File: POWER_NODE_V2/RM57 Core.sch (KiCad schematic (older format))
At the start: 4 parts, among them J5 Booster_J1_J3, J6 I2C2_J10_8_9, J7 Booster_J4_J2

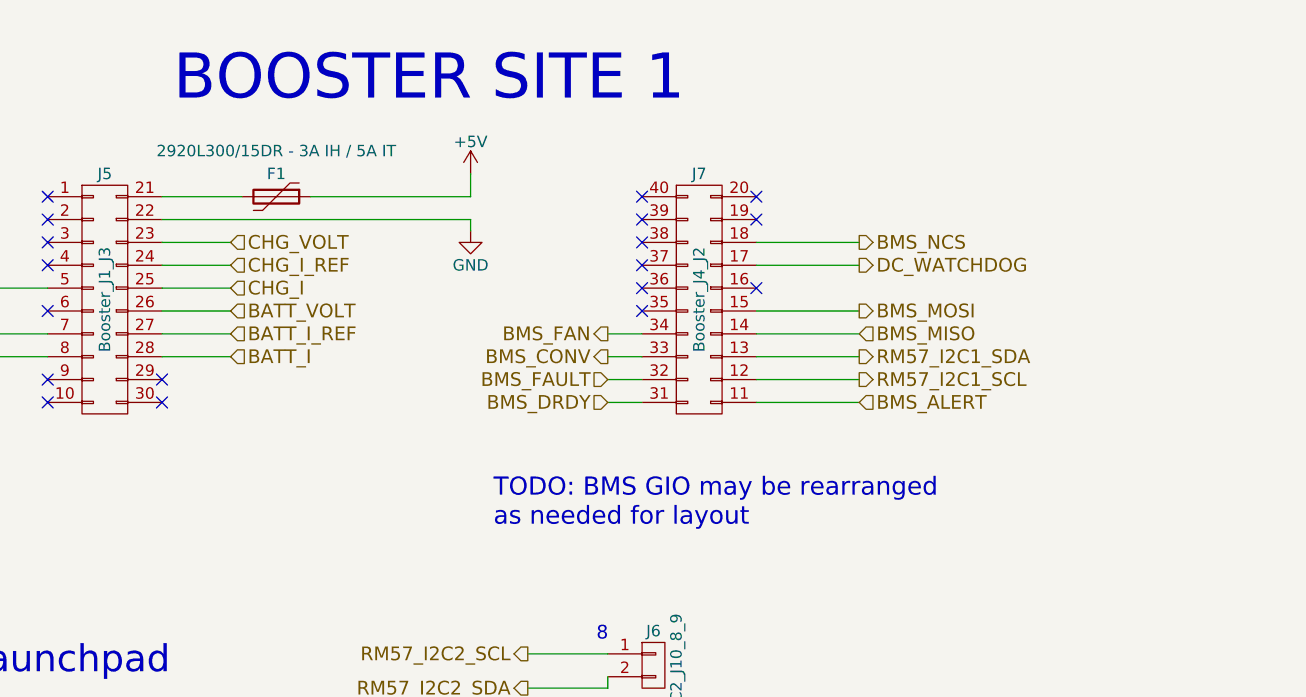
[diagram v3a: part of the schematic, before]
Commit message: Power Node v2 WIP
TODO: 3d models, double check everything, update connector P/N on
schematics, align boards and drill holes
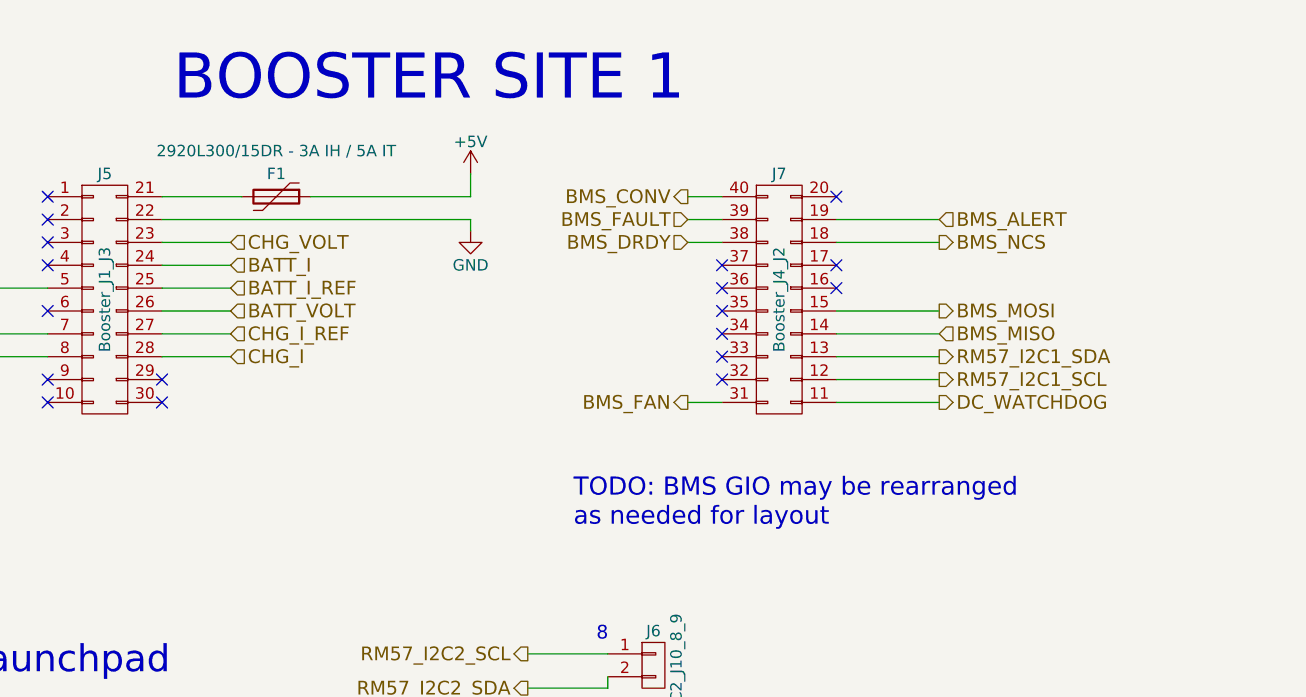
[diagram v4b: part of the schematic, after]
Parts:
- J5: footprint Pin_Headers:Pin_Header_Straight_2x10_Pitch2.54mm -> rLoop Footprints:Booster1_Header_J1_J3
- J6: footprint Pin_Headers:Pin_Header_Straight_1x02_Pitch2.54mm -> Pin_Headers:Pin_Header_Straight_1x02_Pitch2.54mm_SMD_Pin1Left
- J7: footprint Pin_Headers:Pin_Header_Straight_2x10_Pitch2.54mm -> rLoop Footprints:Booster1_J4_J2
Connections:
- net BATT_I: now also J5.24 (P24); no longer J5.28 (P28)
- net BATT_I_REF: now also J5.25 (P25); no longer J5.27 (P27)
- net BMS_ALERT: now also J7.19 (P19); no longer J7.11 (P11)
- net BMS_CONV: now also J7.40 (P40); no longer J7.33 (P33)
- net BMS_DRDY: now also J7.38 (P38); no longer J7.31 (P31)
- net BMS_FAN: now also J7.31 (P31); no longer J7.34 (P34)
- net BMS_FAULT: now also J7.39 (P39); no longer J7.32 (P32)
- net CHG_I: now also J5.28 (P28); no longer J5.25 (P25)
- net CHG_I_REF: now also J5.27 (P27); no longer J5.24 (P24)
- net DC_WATCHDOG: now also J7.11 (P11); no longer J7.17 (P17)
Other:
- moved on the sheet: J7
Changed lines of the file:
@@
 Text HLabel 3700 3200 0    60   Output ~ 0
 CHG_RLY
-Text HLabel 5200 2800 2    60   Input ~ 0
+Text HLabel 5200 3100 2    60   Input ~ 0
 CHG_I_REF
 Text HLabel 5200 2700 2    60   Input ~ 0
@@
 Text HLabel 5200 3000 2    60   Input ~ 0
 BATT_VOLT
-Text HLabel 7950 2800 2    60   Output ~ 0
+Text HLabel 8300 3400 2    60   Output ~ 0
 DC_WATCHDOG
 Text HLabel 3700 3100 0    60   Output ~ 0
 BMS_SCK
-Text HLabel 7950 3000 2    60   Output ~ 0
+Text HLabel 8300 3000 2    60   Output ~ 0
 BMS_MOSI
-Text HLabel 7950 2700 2    60   Output ~ 0
+Text HLabel 8300 2700 2    60   Output ~ 0
 BMS_NCS
-Text HLabel 7950 3100 2    60   Input ~ 0
+Text HLabel 8300 3100 2    60   Input ~ 0
 BMS_MISO
-Text HLabel 6850 3400 0    60   Input ~ 0
+Text HLabel 7200 2700 0    60   Input ~ 0
 BMS_DRDY
 Text HLabel 3700 2900 0    60   Output ~ 0
 BMS_COMMS_EN
-Text HLabel 6850 3200 0    60   Output ~ 0
+Text HLabel 7200 2500 0    60   Output ~ 0
 BMS_CONV
-Text HLabel 7950 3200 2    60   Output ~ 0
+Text HLabel 8300 3200 2    60   Output ~ 0
 RM57_I2C1_SDA
-Text HLabel 7950 3300 2    60   Output ~ 0
+Text HLabel 8300 3300 2    60   Output ~ 0
 RM57_I2C1_SCL
 Text HLabel 6500 4650 0    60   Output ~ 0
@@
 Text HLabel 6500 4500 0    60   Output ~ 0
 RM57_I2C2_SCL
-Text HLabel 6850 3100 0    60   Output ~ 0
+Text HLabel 7200 3400 0    60   Output ~ 0
 BMS_FAN
-Text HLabel 6850 3300 0    60   Input ~ 0
+Text HLabel 7200 2600 0    60   Input ~ 0
 BMS_FAULT
-Text HLabel 7950 3400 2    60   Input ~ 0
+Text HLabel 8300 2600 2    60   Input ~ 0
 BMS_ALERT
 $Comp
@@
 F 0 "J6" H 7050 4700 50  0000 C CNN
 F 1 "I2C2_J10_8_9" V 7150 4550 50  0000 C CNN
-F 2 "Pin_Headers:Pin_Header_Straight_1x02_Pitch2.54mm" H 7050 4550 50  0001 C CNN
+F 2 "Pin_Headers:Pin_Header_Straight_1x02_Pitch2.54mm_SMD_Pin1Left" H 7050 4550 50  0001 C CNN
 F 3 "" H 7050 4550 50  0001 C CNN
 	1    7050 4550
@@
 F 0 "J5" H 4650 3500 50  0000 C CNN
 F 1 "Booster_J1_J3" V 4650 2950 50  0000 C CNN
-F 2 "Pin_Headers:Pin_Header_Straight_2x10_Pitch2.54mm" H 4650 1750 50  0001 C CNN
+F 2 "rLoop Footprints:Booster1_Header_J1_J3" H 4650 1750 50  0001 C CNN
 F 3 "" H 4650 1750 50  0001 C CNN
 	1    4650 2950
 	1    0    0    -1
 $EndComp
-$Comp
-L Booster_J4_J2 J7
-U 1 1 5950B1BF
-P 7250 2950
-F 0 "J7" H 7250 3500 50  0000 C CNN
-F 1 "Booster_J4_J2" V 7250 2950 50  0000 C CNN
-F 2 "Pin_Headers:Pin_Header_Straight_2x10_Pitch2.54mm" H 7250 1750 50  0001 C CNN
-F 3 "" H 7250 1750 50  0001 C CNN
-	1    7250 2950
-	1    0    0    -1
-$EndComp
-Wire Wire Line
-	7950 3300 7500 3300
-Wire Wire Line
-	7500 3200 7950 3200
-Wire Wire Line
-	7950 3100 7500 3100
-Wire Wire Line
-	7500 3000 7950 3000
-Wire Wire Line
-	7950 2700 7500 2700
+Wire Wire Line
+	8300 3300 7850 3300
+Wire Wire Line
+	8300 3100 7850 3100
+Wire Wire Line
+	7850 3000 8300 3000
+Wire Wire Line
+	8300 2700 7850 2700
 Wire Wire Line
 	3700 3100 4400 3100
@@
 Text Notes 6800 4800 0    60   ~ 0
 9
+Text HLabel 5200 3200 2    60   Input ~ 0
+CHG_I
 Text HLabel 5200 2900 2    60   Input ~ 0
-CHG_I
-Text HLabel 5200 3100 2    60   Input ~ 0
 BATT_I_REF
-Text HLabel 5200 3200 2    60   Input ~ 0
+Text HLabel 5200 2800 2    60   Input ~ 0
 BATT_I
-Text Notes 6350 3950 0    79   ~ 0
+Text Notes 6700 3950 0    79   ~ 0
 TODO: BMS GIO may be rearranged\nas needed for layout
 Wire Wire Line
-	6850 3100 7000 3100
-Wire Wire Line
-	7000 3200 6850 3200
-Wire Wire Line
-	6850 3300 7000 3300
-Wire Wire Line
-	7000 3400 6850 3400
-Wire Wire Line
-	7500 3400 7950 3400
-Wire Wire Line
-	4900 3200 5200 3200
-Wire Wire Line
-	5200 3100 4900 3100
-Wire Wire Line
 	4900 3000 5200 3000
-Wire Wire Line
-	5200 2900 4900 2900
-Wire Wire Line
-	4900 2800 5200 2800
-Wire Wire Line
-	5200 2700 4900 2700
-Wire Wire Line
-	7950 2800 7500 2800
 Wire Wire Line
 	3700 2900 4400 2900
@@
 	1    0    0    -1
 $EndComp
-NoConn ~ 7000 3000
-NoConn ~ 7000 2900
-NoConn ~ 7000 2800
-NoConn ~ 7000 2700
-NoConn ~ 7000 2600
-NoConn ~ 7000 2500
-NoConn ~ 7500 2500
-NoConn ~ 7500 2600
-NoConn ~ 7500 2900
+NoConn ~ 7350 3000
+NoConn ~ 7350 2900
+NoConn ~ 7850 2500
+NoConn ~ 7850 2900
 $Comp
 L Polyfuse F1
@@
 Text Notes 2900 4600 0    118  ~ 0
 J9 Pins 8,9 on Launchpad
+Wire Wire Line
+	5200 2700 4900 2700
+Wire Wire Line
+	5200 2800 4900 2800
+Wire Wire Line
+	4900 2900 5200 2900
+Wire Wire Line
+	5200 3100 4900 3100
+Wire Wire Line
+	4900 3200 5200 3200
+Wire Wire Line
+	7850 3200 8300 3200
+Wire Wire Line
+	7850 2600 8300 2600
+Wire Wire Line
+	7200 2500 7350 2500
+Wire Wire Line
+	7350 2600 7200 2600
+Wire Wire Line
+	7200 2700 7350 2700
+NoConn ~ 7850 2800
+Wire Wire Line
+	7850 3400 8300 3400
+NoConn ~ 7350 3200
+NoConn ~ 7350 3300
+$Comp
+L Booster_J4_J2 J7
+U 1 1 5950B1BF
+P 7600 2950
+F 0 "J7" H 7600 3500 50  0000 C CNN
+F 1 "Booster_J4_J2" V 7600 2950 50  0000 C CNN
+F 2 "rLoop Footprints:Booster1_J4_J2" H 7600 1750 50  0001 C CNN
+F 3 "" H 7600 1750 50  0001 C CNN
+	1    7600 2950
+	1    0    0    -1
+$EndComp
+Wire Wire Line
+	7200 3400 7350 3400
+NoConn ~ 7350 3100
+NoConn ~ 7350 2800
 $EndSCHEMATC

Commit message: Lot's of progress
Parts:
- J5: value Booster_J1_J3 -> 5-146130-9; footprint rLoop Footprints:Booster1_Header_J1_J3 -> rLoop_Footprints:Booster1_Header_J1_J3
- J7: value Booster_J4_J2 -> 5-146130-9; footprint rLoop Footprints:Booster1_J4_J2 -> rLoop_Footprints:Booster1_J4_J2
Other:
- note added: "J1 & J3"
- note added: "J2 & J4"
- note removed: "TODO: BMS GIO may be rearranged\nas needed for layout"
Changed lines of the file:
@@
 P 4650 2950
 F 0 "J5" H 4650 3500 50  0000 C CNN
-F 1 "Booster_J1_J3" V 4650 2950 50  0000 C CNN
-F 2 "rLoop Footprints:Booster1_Header_J1_J3" H 4650 1750 50  0001 C CNN
+F 1 "5-146130-9" V 4650 2950 50  0000 C CNN
+F 2 "rLoop_Footprints:Booster1_Header_J1_J3" H 4650 1750 50  0001 C CNN
 F 3 "" H 4650 1750 50  0001 C CNN
 	1    4650 2950
@@
 Text HLabel 5200 2800 2    60   Input ~ 0
 BATT_I
-Text Notes 6700 3950 0    79   ~ 0
-TODO: BMS GIO may be rearranged\nas needed for layout
 Wire Wire Line
 	4900 3000 5200 3000
@@
 P 7600 2950
 F 0 "J7" H 7600 3500 50  0000 C CNN
-F 1 "Booster_J4_J2" V 7600 2950 50  0000 C CNN
-F 2 "rLoop Footprints:Booster1_J4_J2" H 7600 1750 50  0001 C CNN
+F 1 "5-146130-9" V 7600 2950 50  0000 C CNN
+F 2 "rLoop_Footprints:Booster1_J4_J2" H 7600 1750 50  0001 C CNN
 F 3 "" H 7600 1750 50  0001 C CNN
 	1    7600 2950
@@
 NoConn ~ 7350 3100
 NoConn ~ 7350 2800
+Text Notes 4450 3600 0    60   ~ 0
+J1 & J3
+Text Notes 7400 3600 0    60   ~ 0
+J2 & J4
 $EndSCHEMATC

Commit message: All modelled, schematics and mechanical just need a double check
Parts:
- F1: footprint rLoop Footprints:2920L300_15DR -> rLoop_Footprints:2920L300_15DR
- J6: value I2C2_J10_8_9 -> 826926-2; footprint Pin_Headers:Pin_Header_Straight_1x02_Pitch2.54mm_SMD_Pin1Left -> Pin_Headers:Pin_Header_Straight_1x02_Pitch2.54mm
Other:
- note added: "I2C_J10_8_9"
- note added: "Install 215299-2 on Launchpad"
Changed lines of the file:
@@
 P 7050 4550
 F 0 "J6" H 7050 4700 50  0000 C CNN
-F 1 "I2C2_J10_8_9" V 7150 4550 50  0000 C CNN
-F 2 "Pin_Headers:Pin_Header_Straight_1x02_Pitch2.54mm_SMD_Pin1Left" H 7050 4550 50  0001 C CNN
+F 1 "826926-2" V 7150 4550 50  0000 C CNN
+F 2 "Pin_Headers:Pin_Header_Straight_1x02_Pitch2.54mm" H 7050 4550 50  0001 C CNN
 F 3 "" H 7050 4550 50  0001 C CNN
 	1    7050 4550
@@
 NoConn ~ 4900 3300
 $Comp
-L +5V #PWR030
+L +5V #PWR029
 U 1 1 59521447
 P 6250 2400
-F 0 "#PWR030" H 6250 2250 50  0001 C CNN
+F 0 "#PWR029" H 6250 2250 50  0001 C CNN
 F 1 "+5V" H 6250 2540 50  0000 C CNN
 F 2 "" H 6250 2400 50  0001 C CNN
@@
 F 0 "F1" V 5300 2500 50  0000 C CNN
 F 1 "2920L300/15DR - 3A IH / 5A IT" V 5200 2500 50  0000 C CNN
-F 2 "rLoop Footprints:2920L300_15DR" H 5450 2300 50  0001 L CNN
+F 2 "rLoop_Footprints:2920L300_15DR" H 5450 2300 50  0001 L CNN
 F 3 "" H 5400 2500 50  0001 C CNN
 	1    5400 2500
@@
 	6250 2500 6250 2400
 $Comp
-L GND #PWR031
+L GND #PWR030
 U 1 1 59521ACA
 P 6250 2650
-F 0 "#PWR031" H 6250 2400 50  0001 C CNN
+F 0 "#PWR030" H 6250 2400 50  0001 C CNN
 F 1 "GND" H 6250 2500 50  0000 C CNN
 F 2 "" H 6250 2650 50  0001 C CNN
@@
 Text Notes 7400 3600 0    60   ~ 0
 J2 & J4
+Text Notes 6750 4950 0    60   ~ 0
+I2C_J10_8_9
+Text Notes 7250 4650 0    60   ~ 0
+Install 215299-2 on Launchpad
 $EndSCHEMATC

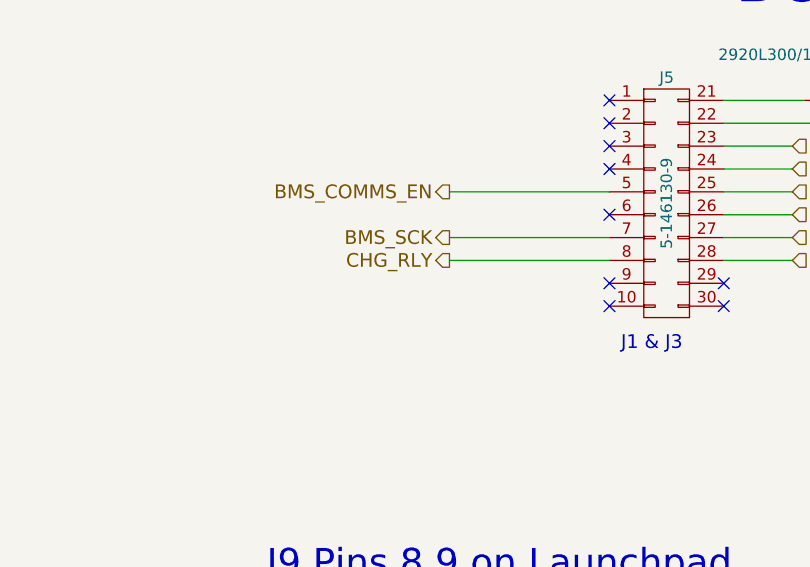
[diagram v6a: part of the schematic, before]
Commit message: Added tooling holes & fiducial marks
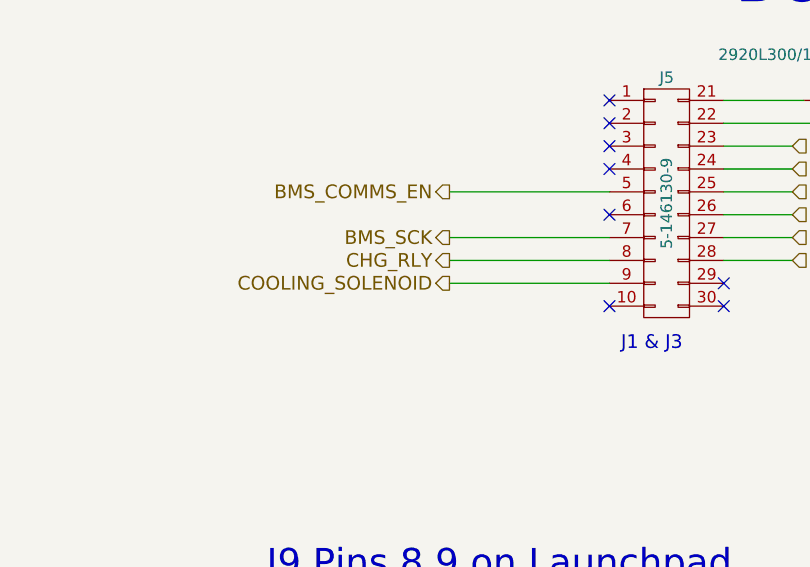
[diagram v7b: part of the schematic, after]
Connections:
- net COOLING_SOLENOID: now reaches J5.9 (P9)
- no-connect marks 18 -> 17
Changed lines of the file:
@@
 EESchema Schematic File Version 2
+LIBS:POWER_NODE_V2-rescue
 LIBS:power
 LIBS:device
@@
 $Descr A4 11693 8268
 encoding utf-8
-Sheet 4 9
+Sheet 4 10
 Title ""
 Date ""
@@
 NoConn ~ 4400 2700
 NoConn ~ 4400 3000
-NoConn ~ 4400 3300
 NoConn ~ 4400 3400
 NoConn ~ 4900 3400
 NoConn ~ 4900 3300
 $Comp
-L +5V #PWR029
+L +5V #PWR29
 U 1 1 59521447
 P 6250 2400
-F 0 "#PWR029" H 6250 2250 50  0001 C CNN
+F 0 "#PWR29" H 6250 2250 50  0001 C CNN
 F 1 "+5V" H 6250 2540 50  0000 C CNN
 F 2 "" H 6250 2400 50  0001 C CNN
@@
 	6250 2500 6250 2400
 $Comp
-L GND #PWR030
+L GND #PWR30
 U 1 1 59521ACA
 P 6250 2650
-F 0 "#PWR030" H 6250 2400 50  0001 C CNN
+F 0 "#PWR30" H 6250 2400 50  0001 C CNN
 F 1 "GND" H 6250 2500 50  0000 C CNN
 F 2 "" H 6250 2650 50  0001 C CNN
@@
 Text Notes 7250 4650 0    60   ~ 0
 Install 215299-2 on Launchpad
+Text HLabel 3700 3300 0    60   Output ~ 0
+COOLING_SOLENOID
+Wire Wire Line
+	3700 3300 4400 3300
 $EndSCHEMATC
